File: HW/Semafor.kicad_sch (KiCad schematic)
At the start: 62 parts, among them J1 USB_C_Receptacle_USB2.0, J2 USB_plug, M1 Motor_DC, Q2 Q_NMOS_GSD, Q3 Q_NMOS_GSD, Q4 Q_NMOS_GSD, SW6 SW_SPDT, U1 ESP32-C3, U2 CN3058E, U3 LT1930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

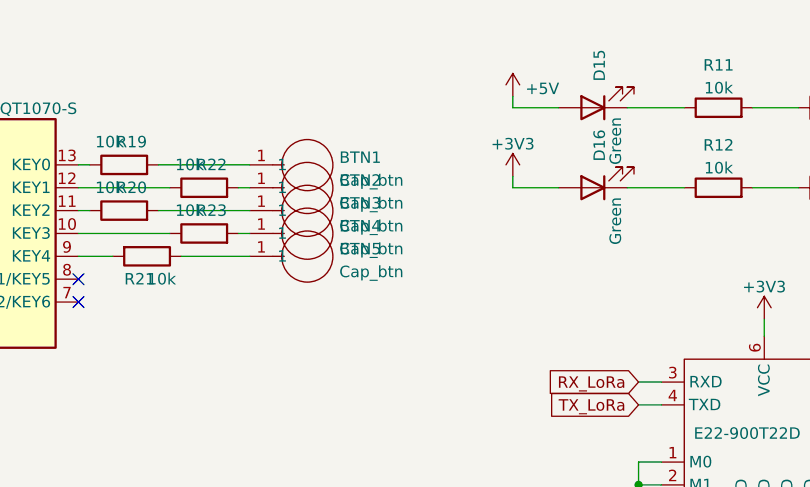
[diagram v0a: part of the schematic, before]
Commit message: update footprints of capacitive touch buttons, PCB
place capacitive buttons, LEDs, LoRa module, battery pack
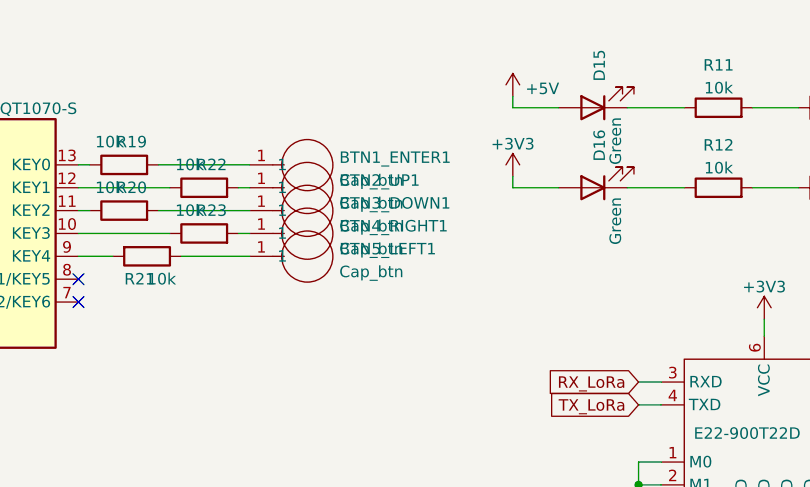
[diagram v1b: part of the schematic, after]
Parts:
- BTN1_ENTER1: renamed from BTN1; footprint Library:Cap_btn -> Library:Cap_btn_5x5
- BTN2_UP1: renamed from BTN2; footprint Library:Cap_btn -> Library:Cap_btn_2x2
- BTN3_DOWN1: renamed from BTN3; footprint Library:Cap_btn -> Library:Cap_btn_2x2
- BTN4_RIGHT1: renamed from BTN4; footprint Library:Cap_btn -> Library:Cap_btn_2x2
- BTN5_LEFT1: renamed from BTN5; footprint Library:Cap_btn -> Library:Cap_btn_2x2
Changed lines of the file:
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@@
   (symbol (lib_id "Library:Cap_btn") (at 214.63 36.83 0) (unit 1)
     (in_bom yes) (on_board yes) (fields_autoplaced)
-    (property "Reference" "BTN3" (id 0) (at 218.2064 36.0207 0)
+    (property "Reference" "BTN3_DOWN1" (id 0) (at 218.2064 36.0207 0)
       (effects (font (size 1.27 1.27)) (justify left))
     )
@@
       (effects (font (size 1.27 1.27)) (justify left))
     )
-    (property "Footprint" "Library:Cap_btn" (id 2) (at 214.6554 40.6654 0)
+    (property "Footprint" "Library:Cap_btn_2x2" (id 2) (at 214.6554 40.6654 0)
       (effects (font (size 1.27 1.27)) hide)
     )
@@
   (symbol (lib_id "Library:Cap_btn") (at 214.63 31.75 0) (unit 1)
     (in_bom yes) (on_board yes) (fields_autoplaced)
-    (property "Reference" "BTN1" (id 0) (at 218.2064 30.9407 0)
+    (property "Reference" "BTN1_ENTER1" (id 0) (at 218.2064 30.9407 0)
       (effects (font (size 1.27 1.27)) (justify left))
     )
@@
       (effects (font (size 1.27 1.27)) (justify left))
     )
-    (property "Footprint" "Library:Cap_btn" (id 2) (at 214.6554 35.5854 0)
+    (property "Footprint" "Library:Cap_btn_5x5" (id 2) (at 214.6554 35.5854 0)
       (effects (font (size 1.27 1.27)) hide)
     )
@@
   (symbol (lib_id "Library:Cap_btn") (at 214.63 39.37 0) (unit 1)
     (in_bom yes) (on_board yes) (fields_autoplaced)
-    (property "Reference" "BTN4" (id 0) (at 218.2064 38.5607 0)
+    (property "Reference" "BTN4_RIGHT1" (id 0) (at 218.2064 38.5607 0)
       (effects (font (size 1.27 1.27)) (justify left))
     )
@@
       (effects (font (size 1.27 1.27)) (justify left))
     )
-    (property "Footprint" "Library:Cap_btn" (id 2) (at 214.6554 43.2054 0)
+    (property "Footprint" "Library:Cap_btn_2x2" (id 2) (at 214.6554 43.2054 0)
       (effects (font (size 1.27 1.27)) hide)
     )
@@
   (symbol (lib_id "Library:Cap_btn") (at 214.63 41.91 0) (unit 1)
     (in_bom yes) (on_board yes) (fields_autoplaced)
-    (property "Reference" "BTN5" (id 0) (at 218.2064 41.1007 0)
+    (property "Reference" "BTN5_LEFT1" (id 0) (at 218.2064 41.1007 0)
       (effects (font (size 1.27 1.27)) (justify left))
     )
@@
       (effects (font (size 1.27 1.27)) (justify left))
     )
-    (property "Footprint" "Library:Cap_btn" (id 2) (at 214.6554 45.7454 0)
+    (property "Footprint" "Library:Cap_btn_2x2" (id 2) (at 214.6554 45.7454 0)
       (effects (font (size 1.27 1.27)) hide)
     )
@@
   (symbol (lib_id "Library:Cap_btn") (at 214.63 34.29 0) (unit 1)
     (in_bom yes) (on_board yes) (fields_autoplaced)
-    (property "Reference" "BTN2" (id 0) (at 218.2064 33.4807 0)
+    (property "Reference" "BTN2_UP1" (id 0) (at 218.2064 33.4807 0)
       (effects (font (size 1.27 1.27)) (justify left))
     )
@@
       (effects (font (size 1.27 1.27)) (justify left))
     )
-    (property "Footprint" "Library:Cap_btn" (id 2) (at 214.6554 38.1254 0)
+    (property "Footprint" "Library:Cap_btn_2x2" (id 2) (at 214.6554 38.1254 0)
       (effects (font (size 1.27 1.27)) hide)
     )
@@
     )
     (path "/68281409-52c5-4f8e-8215-bb8b09652217"
-      (reference "BTN1") (unit 1) (value "Cap_btn") (footprint "Library:Cap_btn")
+      (reference "BTN1_ENTER1") (unit 1) (value "Cap_btn") (footprint "Library:Cap_btn_5x5")
     )
     (path "/e088e96c-5953-47aa-bea0-66eddd726a95"
-      (reference "BTN2") (unit 1) (value "Cap_btn") (footprint "Library:Cap_btn")
+      (reference "BTN2_UP1") (unit 1) (value "Cap_btn") (footprint "Library:Cap_btn_2x2")
     )
     (path "/28980d4e-483f-4acc-8206-ccca4c04030d"
-      (reference "BTN3") (unit 1) (value "Cap_btn") (footprint "Library:Cap_btn")
+      (reference "BTN3_DOWN1") (unit 1) (value "Cap_btn") (footprint "Library:Cap_btn_2x2")
     )
     (path "/6ff85135-9668-43ee-94d4-06020ffb73b8"
-      (reference "BTN4") (unit 1) (value "Cap_btn") (footprint "Library:Cap_btn")
+      (reference "BTN4_RIGHT1") (unit 1) (value "Cap_btn") (footprint "Library:Cap_btn_2x2")
     )
     (path "/a0f00b9c-22ea-453c-ba6a-56a6ffe02e68"
-      (reference "BTN5") (unit 1) (value "Cap_btn") (footprint "Library:Cap_btn")
+      (reference "BTN5_LEFT1") (unit 1) (value "Cap_btn") (footprint "Library:Cap_btn_2x2")
     )
     (path "/5f854d10-1eb7-4d49-8a65-bf8e54333008"

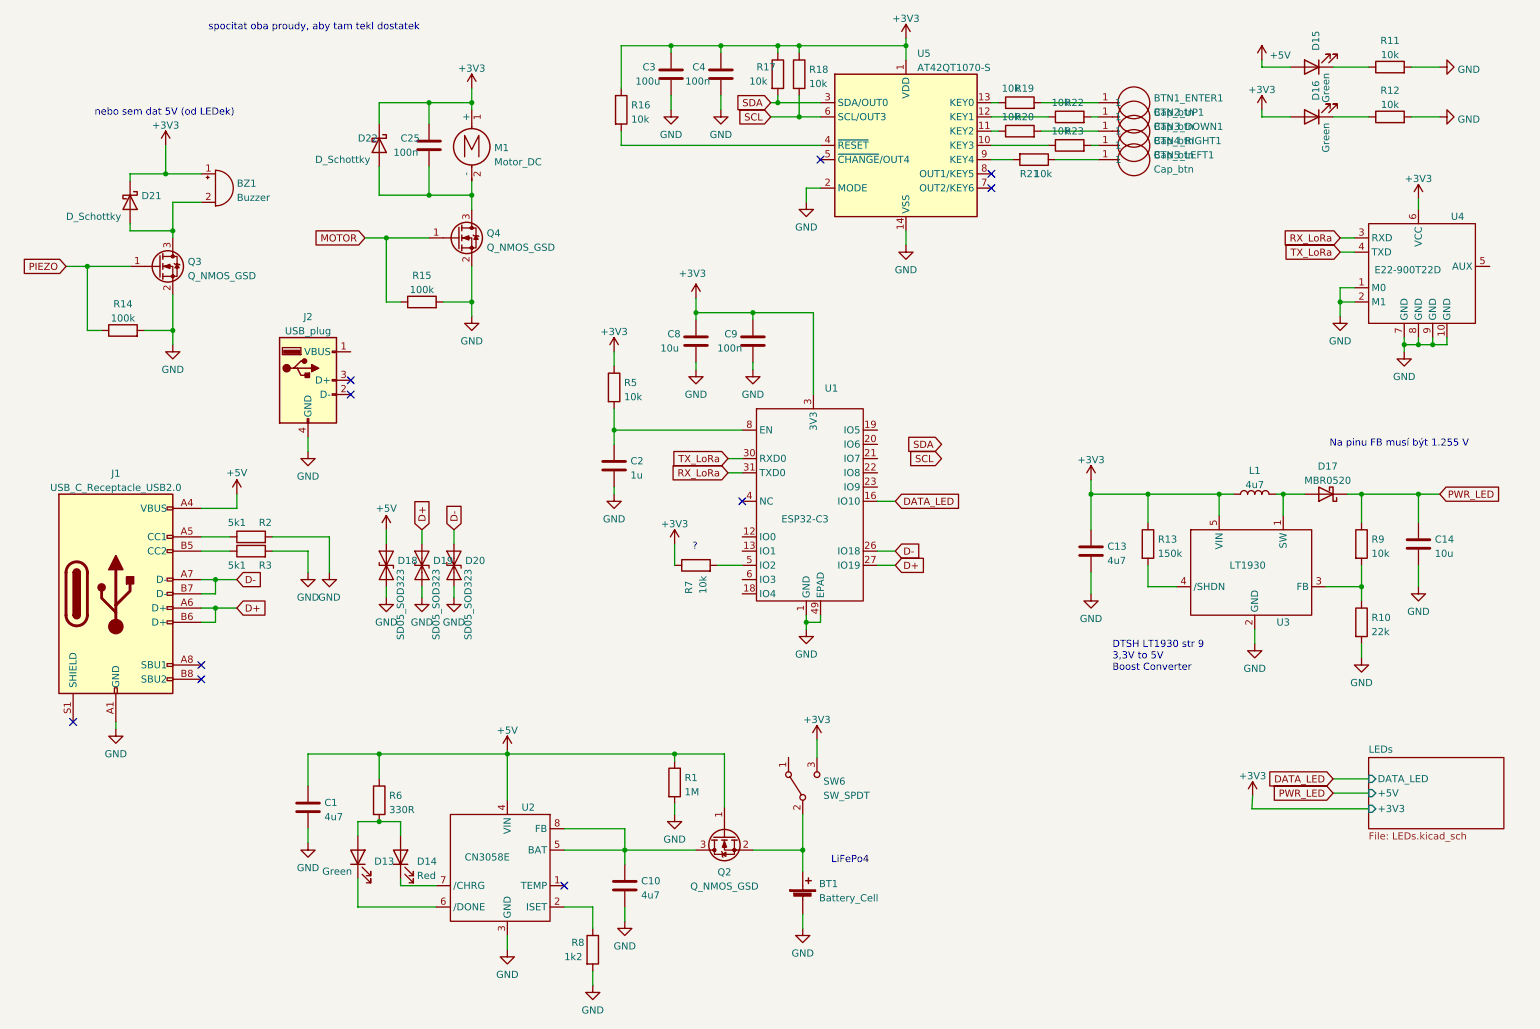
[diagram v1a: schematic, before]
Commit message: add some datasheets, add diodes to USBs
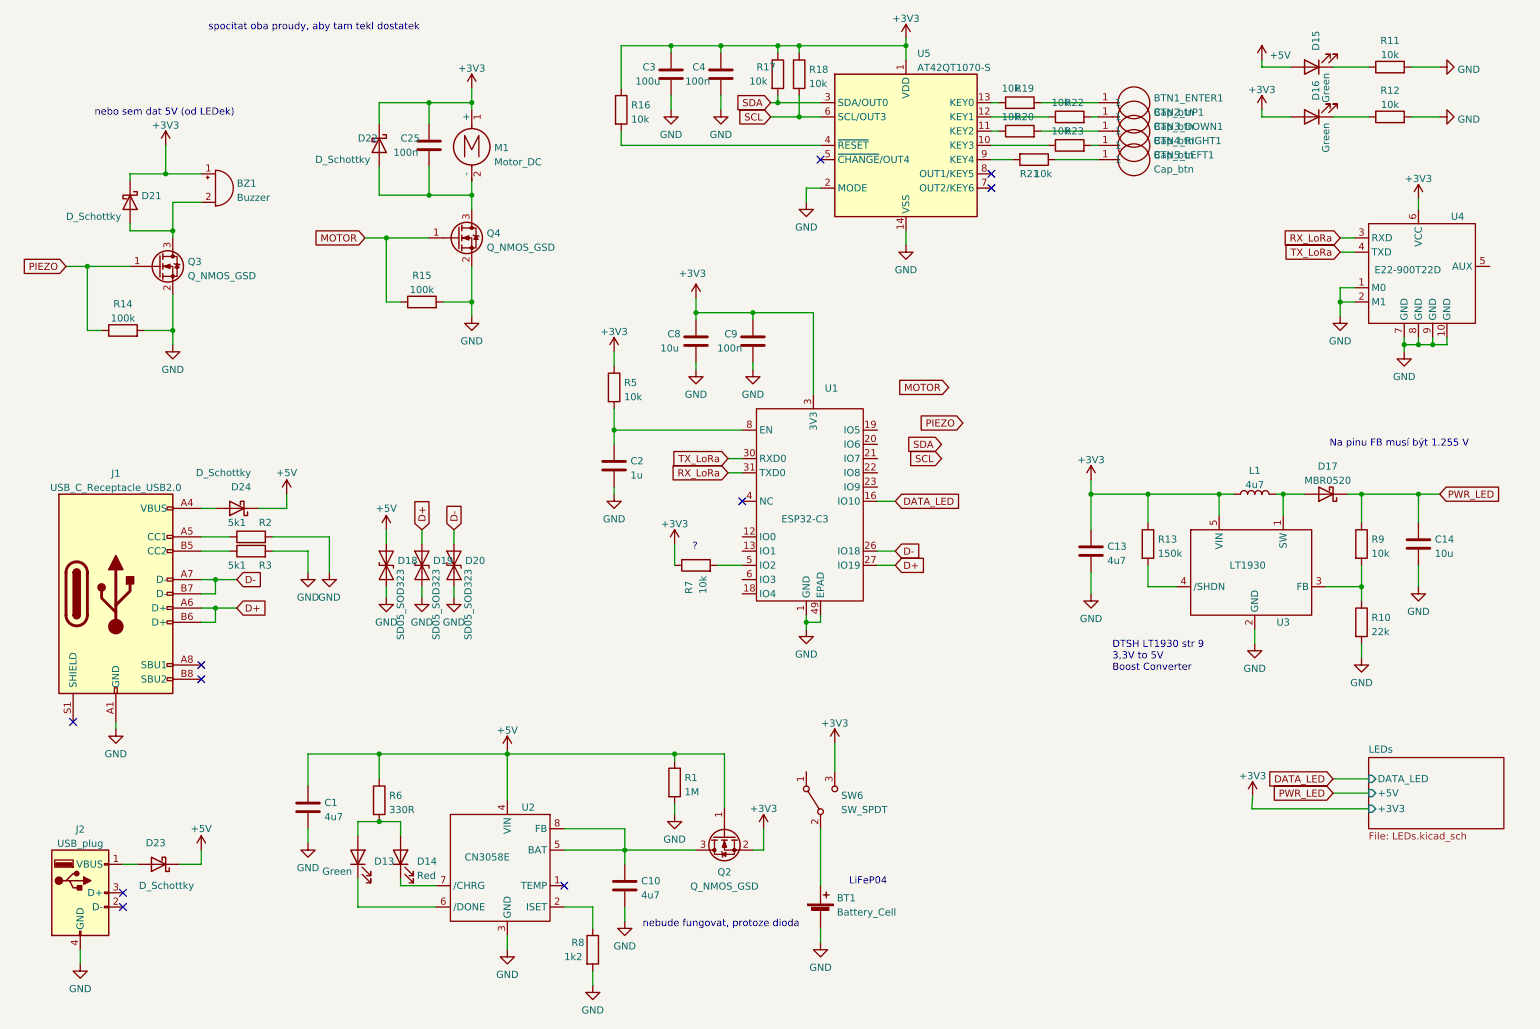
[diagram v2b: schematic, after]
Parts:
- added D23, D24: D_Schottky, Diode_SMD:D_SOD-123, symbol Device:D_Schottky
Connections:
- net +3V3: now also Q2.2 (S)
- net +5V: now also D23.1 (K), D24.1 (K); no longer J1.A4 (VBUS), J1.A9 (VBUS), J1.B4 (VBUS), J1.B9 (VBUS)
- net at BT1.1 (+), SW6.2 (B): no longer Q2.2 (S)
- net at J2.1 (VBUS): now also D23.2 (A)
- new net: D24.2 (A), J1.A4 (VBUS), J1.A9 (VBUS), J1.B4 (VBUS), J1.B9 (VBUS)
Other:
- note added: "LiFeP04"
- note added: "nebude fungovat, protoze dioda"
- note removed: "LiFePo4"
- moved on the sheet: BT1, J2, SW6

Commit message: change datasheet WS2812C, add datasheet LT1930, repair voltage on pin FB of LT1930
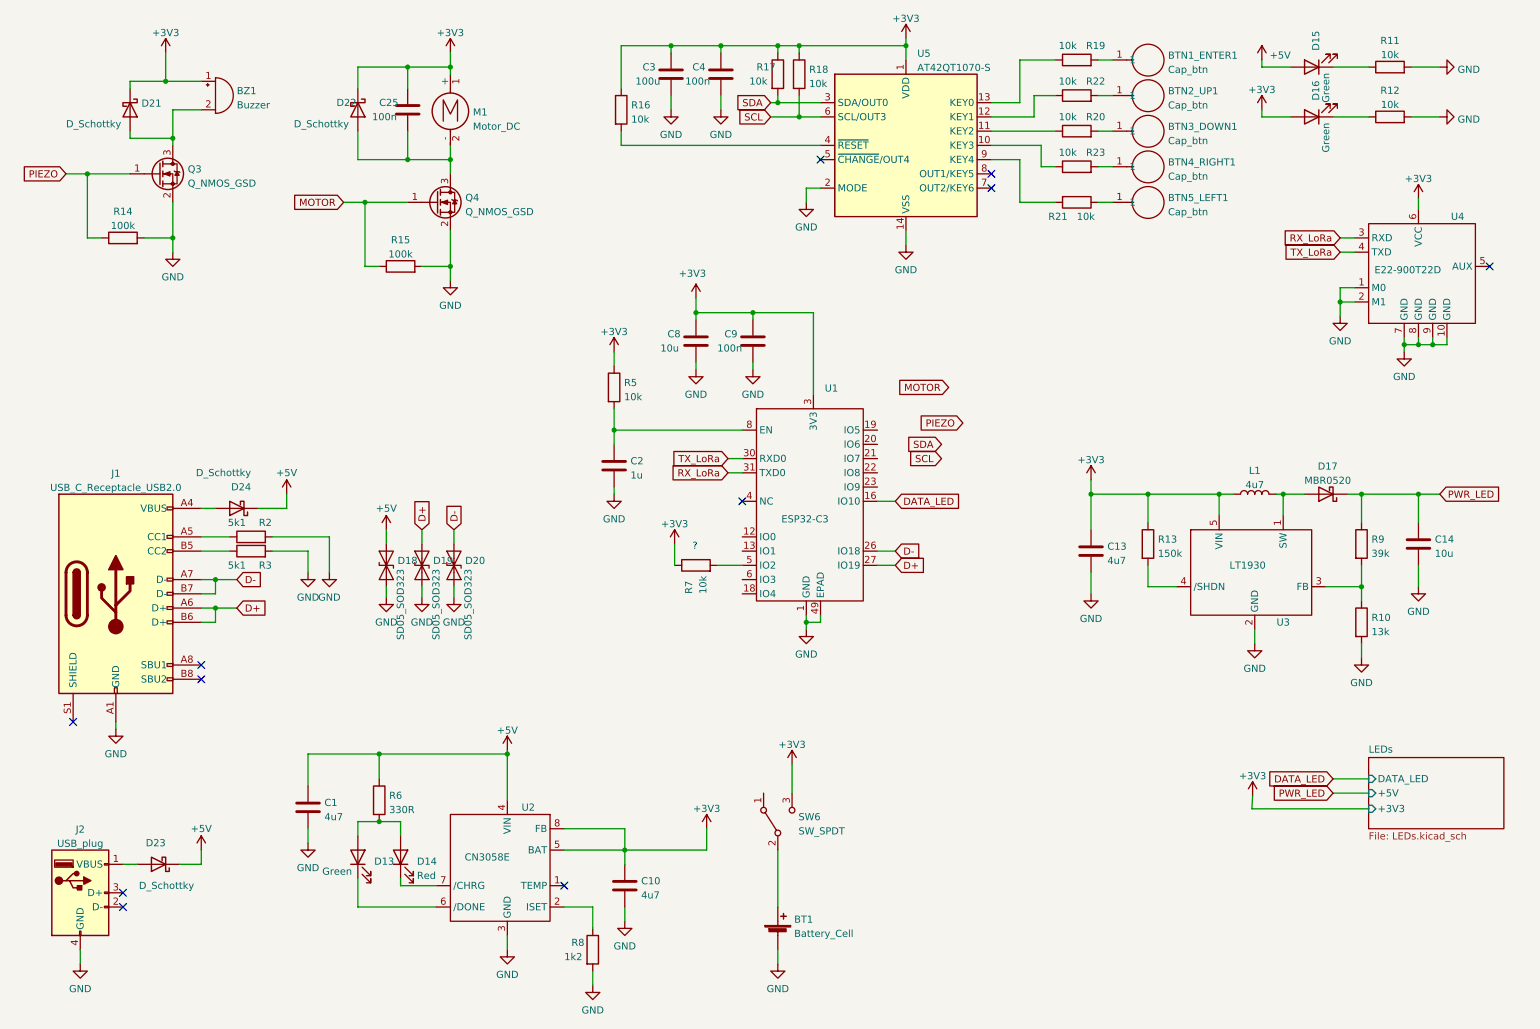
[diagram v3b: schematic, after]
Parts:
- removed Q2: Q_NMOS_GSD, Package_TO_SOT_SMD:SOT-23, symbol Device:Q_NMOS_GSD
- removed R1: 1M, Resistor_SMD:R_0603_1608Metric, symbol Device:R
- R10: value 22k -> 13k
- R9: value 10k -> 39k
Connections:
- net +3V3: now also C10.1, U2.5 (BAT), U2.8 (FB)
- no-connect marks 10 -> 11
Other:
- note removed: "DTSH LT1930 str 9 3,3V to 5V Boost Converter"
- note removed: "LiFeP04"
- note removed: "Na pinu FB musí být 1.255 V"
- note removed: "nebo sem dat 5V (od LEDek)"
- note removed: "nebude fungovat, protoze dioda"
- note removed: "spocitat oba proudy, aby tam tekl dostatek"
- moved on the sheet: BT1, BTN1_ENTER1, BTN2_UP1, BTN3_DOWN1, BTN4_RIGHT1, BTN5_LEFT1, BZ1, C25, D21, D22, M1, Q3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
